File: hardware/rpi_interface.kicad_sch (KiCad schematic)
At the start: 5 parts, among them J14 RPI_Connector, M1 Noctua NF-A4x10

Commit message: First routing draft
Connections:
- net NRST: now also J14.36 (Pin_36); no longer J14.37 (Pin_37)
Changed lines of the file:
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@@
 	)
 	(no_connect
+		(at 142.24 123.19)
+	)
+	(no_connect
 		(at 142.24 97.79)
 	)
@@
 	)
 	(no_connect
-		(at 154.94 120.65)
-	)
-	(no_connect
 		(at 142.24 95.25)
 	)
@@
 		)
 	)
+	(hierarchical_label "NRST"
+		(shape input)
+		(at 154.94 120.65 0)
+		(effects
+			(font
+				(size 1.27 1.27)
+			)
+			(justify left)
+		)
+	)
 	(hierarchical_label "MIC_DOUT"
 		(shape input)
@@
 		)
 	)
-	(hierarchical_label "NRST"
-		(shape input)
-		(at 142.24 123.19 180)
-		(effects
-			(font
-				(size 1.27 1.27)
-			)
-			(justify right)
-		)
-	)

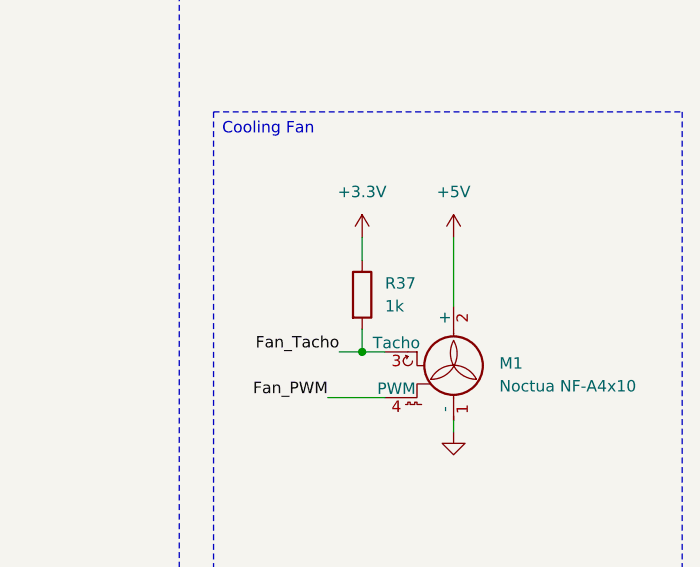
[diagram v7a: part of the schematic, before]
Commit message: Adding external pullup to NRST
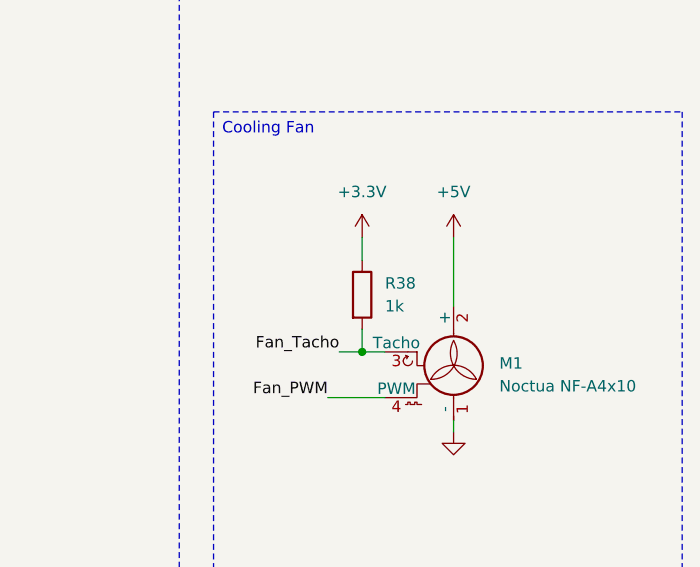
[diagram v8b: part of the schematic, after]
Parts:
- renumbered R37 to R38
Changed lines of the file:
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@@
 		(dnp no)
 		(fields_autoplaced yes)
-		(property "Reference" "#PWR0105"
+		(property "Reference" "#PWR0107"
 			(at 161.29 92.71 0)
 			(hide yes)
@@
 			(project "chromapi_motherboard_v1"
 				(path "/d1a31f26-03e0-43e1-89c1-031fe31befc5/e996aba6-741c-4e73-a7c7-e6548b7ec52f"
-					(reference "#PWR0105")
+					(reference "#PWR0107")
 					(unit 1)
 				)
@@
 		(dnp no)
 		(fields_autoplaced yes)
-		(property "Reference" "#PWR0115"
+		(property "Reference" "#PWR0117"
 			(at 222.25 133.35 0)
 			(hide yes)
@@
 			(project "chromapi_motherboard_v1"
 				(path "/d1a31f26-03e0-43e1-89c1-031fe31befc5/e996aba6-741c-4e73-a7c7-e6548b7ec52f"
-					(reference "#PWR0115")
+					(reference "#PWR0117")
 					(unit 1)
 				)
@@
 		(dnp no)
 		(fields_autoplaced yes)
-		(property "Reference" "#PWR0113"
+		(property "Reference" "#PWR0115"
 			(at 71.12 130.81 0)
 			(hide yes)
@@
 			(project "chromapi_motherboard_v1"
 				(path "/d1a31f26-03e0-43e1-89c1-031fe31befc5/e996aba6-741c-4e73-a7c7-e6548b7ec52f"
-					(reference "#PWR0113")
+					(reference "#PWR0115")
 					(unit 1)
 				)
@@
 		(dnp no)
 		(fields_autoplaced yes)
-		(property "Reference" "#PWR0104"
+		(property "Reference" "#PWR0106"
 			(at 135.89 87.63 0)
 			(hide yes)
@@
 			(project "chromapi_motherboard_v1"
 				(path "/d1a31f26-03e0-43e1-89c1-031fe31befc5/e996aba6-741c-4e73-a7c7-e6548b7ec52f"
-					(reference "#PWR0104")
+					(reference "#PWR0106")
 					(unit 1)
 				)
@@
 		(dnp no)
 		(fields_autoplaced yes)
-		(property "Reference" "R37"
+		(property "Reference" "R38"
 			(at 214.63 110.4899 0)
 			(show_name no)
@@
 			(project "chromapi_motherboard_v1"
 				(path "/d1a31f26-03e0-43e1-89c1-031fe31befc5/e996aba6-741c-4e73-a7c7-e6548b7ec52f"
-					(reference "R37")
+					(reference "R38")
 					(unit 1)
 				)
@@
 		(in_pos_files yes)
 		(dnp no)
-		(property "Reference" "#PWR0109"
+		(property "Reference" "#PWR0111"
 			(at 71.12 111.76 0)
 			(hide yes)
@@
 			(project "chromapi_motherboard_v1"
 				(path "/d1a31f26-03e0-43e1-89c1-031fe31befc5/e996aba6-741c-4e73-a7c7-e6548b7ec52f"
-					(reference "#PWR0109")
+					(reference "#PWR0111")
 					(unit 1)
 				)
@@
 		(dnp no)
 		(fields_autoplaced yes)
-		(property "Reference" "#PWR0114"
+		(property "Reference" "#PWR0116"
 			(at 135.89 125.73 0)
 			(hide yes)
@@
 			(project "chromapi_motherboard_v1"
 				(path "/d1a31f26-03e0-43e1-89c1-031fe31befc5/e996aba6-741c-4e73-a7c7-e6548b7ec52f"
-					(reference "#PWR0114")
+					(reference "#PWR0116")
 					(unit 1)
 				)
@@
 		(dnp no)
 		(fields_autoplaced yes)
-		(property "Reference" "#PWR0102"
+		(property "Reference" "#PWR0104"
 			(at 161.29 77.47 0)
 			(hide yes)
@@
 			(project "chromapi_motherboard_v1"
 				(path "/d1a31f26-03e0-43e1-89c1-031fe31befc5/e996aba6-741c-4e73-a7c7-e6548b7ec52f"
-					(reference "#PWR0102")
+					(reference "#PWR0104")
 					(unit 1)
 				)
@@
 		(dnp no)
 		(fields_autoplaced yes)
-		(property "Reference" "#PWR0103"
+		(property "Reference" "#PWR0105"
 			(at 161.29 82.55 0)
 			(hide yes)
@@
 			(project "chromapi_motherboard_v1"
 				(path "/d1a31f26-03e0-43e1-89c1-031fe31befc5/e996aba6-741c-4e73-a7c7-e6548b7ec52f"
-					(reference "#PWR0103")
+					(reference "#PWR0105")
 					(unit 1)
 				)
@@
 		(dnp no)
 		(fields_autoplaced yes)
-		(property "Reference" "#PWR0112"
+		(property "Reference" "#PWR0114"
 			(at 161.29 118.11 0)
 			(hide yes)
@@
 			(project "chromapi_motherboard_v1"
 				(path "/d1a31f26-03e0-43e1-89c1-031fe31befc5/e996aba6-741c-4e73-a7c7-e6548b7ec52f"
-					(reference "#PWR0112")
+					(reference "#PWR0114")
 					(unit 1)
 				)
@@
 		(dnp no)
 		(fields_autoplaced yes)
-		(property "Reference" "#PWR0111"
+		(property "Reference" "#PWR0113"
 			(at 161.29 113.03 0)
 			(hide yes)
@@
 			(project "chromapi_motherboard_v1"
 				(path "/d1a31f26-03e0-43e1-89c1-031fe31befc5/e996aba6-741c-4e73-a7c7-e6548b7ec52f"
-					(reference "#PWR0111")
+					(reference "#PWR0113")
 					(unit 1)
 				)
@@
 		(dnp no)
 		(fields_autoplaced yes)
-		(property "Reference" "#PWR0108"
+		(property "Reference" "#PWR0110"
 			(at 222.25 109.22 0)
 			(hide yes)
@@
 			(project "chromapi_motherboard_v1"
 				(path "/d1a31f26-03e0-43e1-89c1-031fe31befc5/e996aba6-741c-4e73-a7c7-e6548b7ec52f"
-					(reference "#PWR0108")
+					(reference "#PWR0110")
 					(unit 1)
 				)
@@
 		(dnp no)
 		(fields_autoplaced yes)
-		(property "Reference" "#PWR0106"
+		(property "Reference" "#PWR0108"
 			(at 161.29 100.33 0)
 			(hide yes)
@@
 			(project "chromapi_motherboard_v1"
 				(path "/d1a31f26-03e0-43e1-89c1-031fe31befc5/e996aba6-741c-4e73-a7c7-e6548b7ec52f"
-					(reference "#PWR0106")
+					(reference "#PWR0108")
 					(unit 1)
 				)
@@
 		(dnp no)
 		(fields_autoplaced yes)
-		(property "Reference" "#PWR0107"
+		(property "Reference" "#PWR0109"
 			(at 212.09 109.22 0)
 			(hide yes)
@@
 			(project "chromapi_motherboard_v1"
 				(path "/d1a31f26-03e0-43e1-89c1-031fe31befc5/e996aba6-741c-4e73-a7c7-e6548b7ec52f"
-					(reference "#PWR0107")
+					(reference "#PWR0109")
 					(unit 1)
 				)
@@
 		(dnp no)
 		(fields_autoplaced yes)
-		(property "Reference" "#PWR0110"
+		(property "Reference" "#PWR0112"
 			(at 135.89 107.95 0)
 			(hide yes)
@@
 			(project "chromapi_motherboard_v1"
 				(path "/d1a31f26-03e0-43e1-89c1-031fe31befc5/e996aba6-741c-4e73-a7c7-e6548b7ec52f"
-					(reference "#PWR0110")
-					(unit 1)
-				)
+					(reference "#PWR0112")
+					(unit 1)
+				)
